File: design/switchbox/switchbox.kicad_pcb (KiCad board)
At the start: 2 copper layers, 70 x 32 mm, 7 parts, among them J1 A0, J2 GND, SW1 SW_Push, SW2 SW_Push

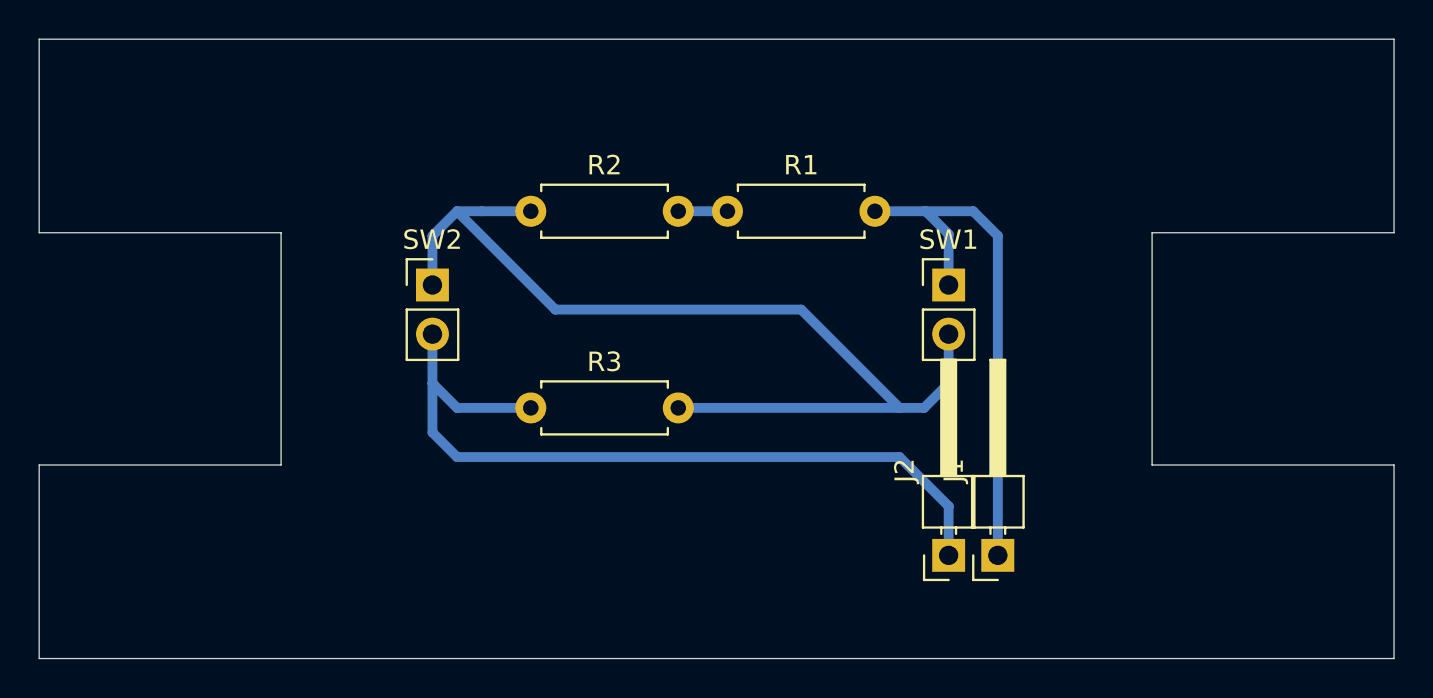
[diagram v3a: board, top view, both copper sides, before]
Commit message: Added filled areas
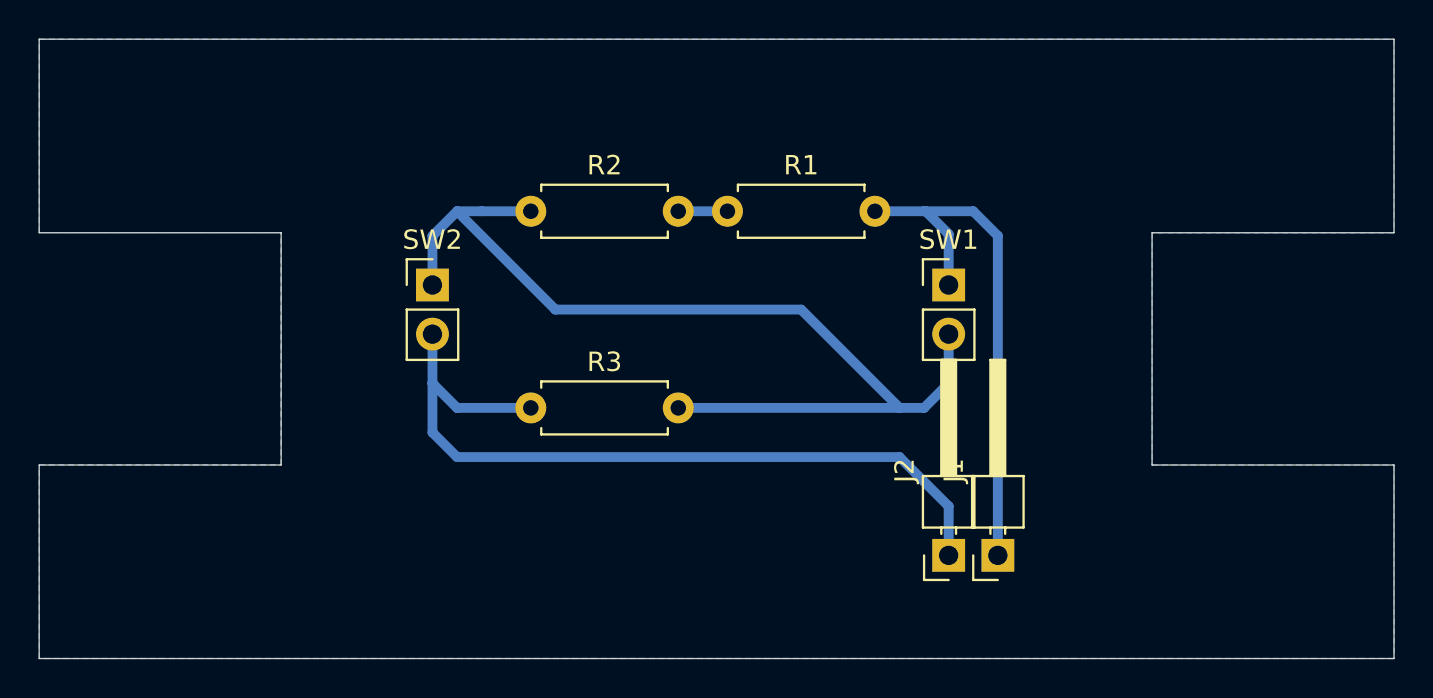
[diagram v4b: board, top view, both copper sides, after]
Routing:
- added copper zone on B.Cu, net (none)
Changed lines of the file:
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@@
   )
   (setup
-    (last_trace_width 0.508)
+    (last_trace_width 0.25)
     (user_trace_width 0.381)
     (user_trace_width 0.508)
@@
   (segment (start 137.16 91.44) (end 137.16 88.9) (width 0.508) (layer B.Cu) (net 4))
   (segment (start 163.83 97.79) (end 163.83 95.25) (width 0.508) (layer B.Cu) (net 4))
+  (zone (net 0) (net_name "") (layer B.Cu) (hatch edge 0.508)
+    (connect_pads (clearance 0.508))
+    (min_thickness 0.254)
+    (fill yes (arc_segments 32) (thermal_gap 0.508) (thermal_bridge_width 0.508))
+    (polygon
+      (pts
+        (xy 186.837861 71.12249) (xy 186.838428 81.122913) (xy 174.342675 81.122913) (xy 174.342458 93.122508) (xy 186.838791 93.122508)
+        (xy 186.840068 103.117169) (xy 116.84 103.117169) (xy 116.84 93.115481) (xy 129.339612 93.115481) (xy 129.339612 81.11869)
+        (xy 116.84 81.11869) (xy 116.84 71.12)
+      )
+    )
+  )
 )

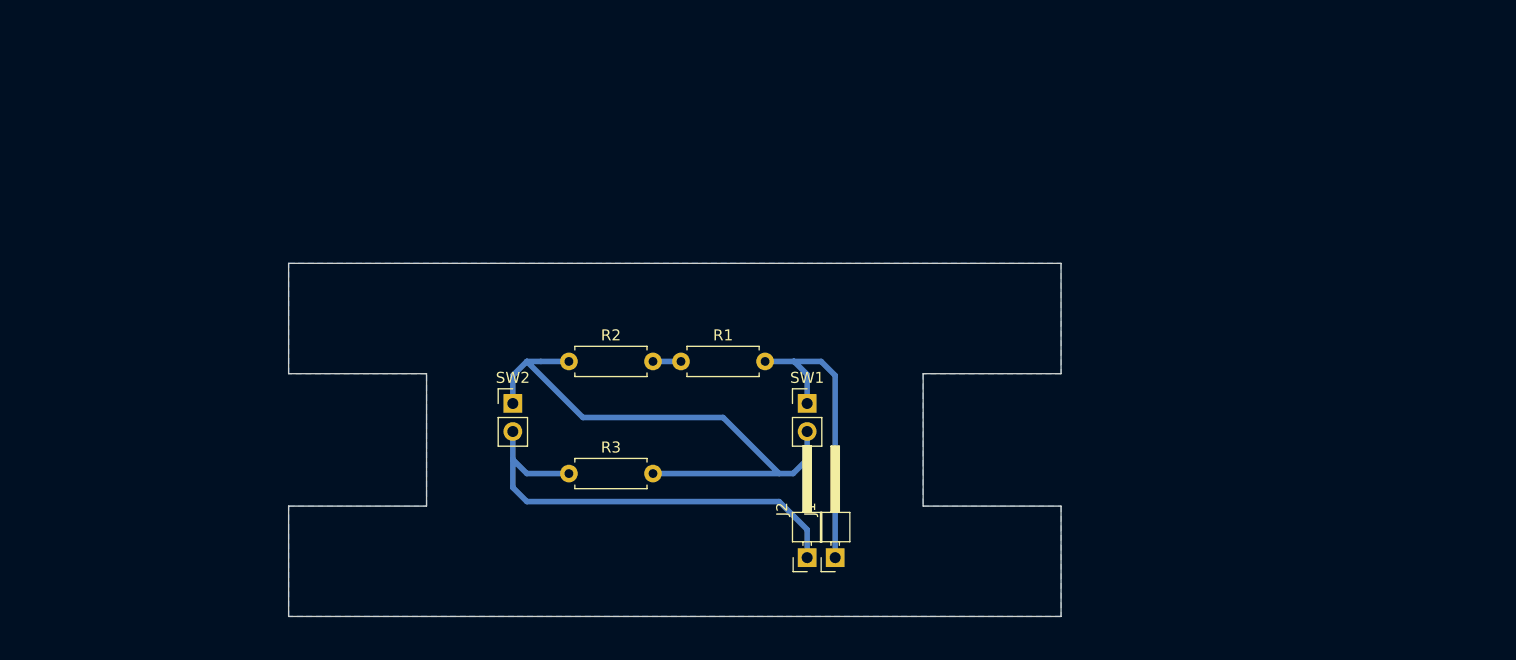
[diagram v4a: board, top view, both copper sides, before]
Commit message: Updated footprints and front size texts
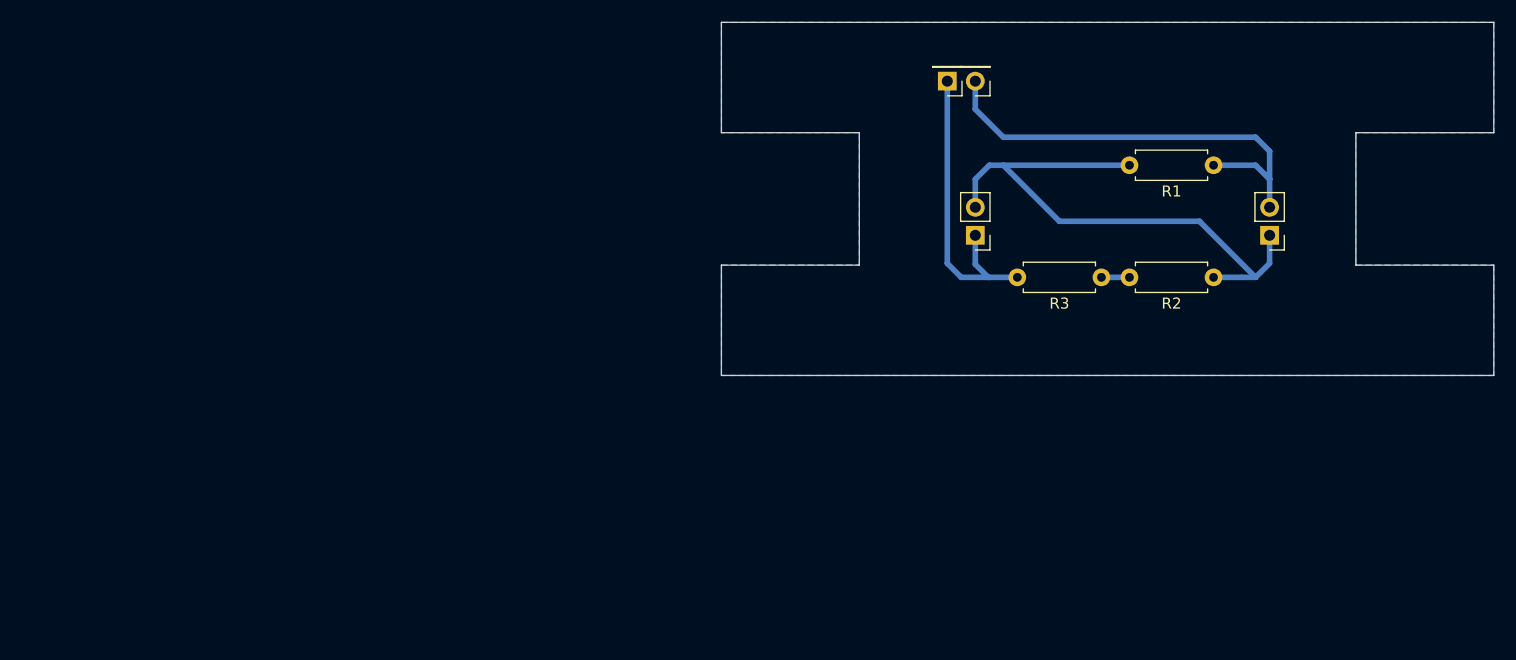
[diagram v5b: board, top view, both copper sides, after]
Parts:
- J1, J2: footprint Connector_PinHeader_2.54mm:PinHeader_1x01_P2.54mm_Horizontal -> Connector_PinHeader_2.54mm:PinHeader_1x01_P2.54mm_Vertical
- SW1: renamed from SW2; value SW_Push -> SW1
- SW2: renamed from SW1; value SW_Push -> SW2
- moved SW1 70.3 mm to (205.7, 68.6), turned to 180 degrees
- moved R1 64.8 mm to (200.7, 62.2), turned to 180 degrees
- moved R2 58.9 mm to (200.7, 72.4), turned to 180 degrees
- moved J2 45.8 mm to (179.1, 54.6), turned to 180 degrees
- moved J1 44.4 mm to (176.5, 54.6), turned to 180 degrees
- moved R3 38.9 mm to (190.5, 72.4), turned to 180 degrees
- moved SW2 21.6 mm to (179.1, 68.6), turned to 180 degrees
- renumbered R3 to R1, R1 to R3
